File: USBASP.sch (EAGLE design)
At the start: 25 parts, among them IC1 ATMEGA8, IC2 LD111733, J1 Program, J2 Slow clock, J3 USB, J4 ISP Target, J5 VDD Select, Q1 12 MHz

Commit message: Updates for v1.0 release
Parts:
- removed J5: VDD Select, freetronics-luke:JUMPER_SPDT
- added S1: USB, freetronics-jon:USB-6PSMT
- C3: value 22p 0604 -> 22p 0603
- F1: value 500mA PTC -> 500mA PTC 1812
- J1: value Program -> Slow clock
- J2: value Slow clock -> Program
- J3: value USB -> VDD Select; device freetronics-jon:USB-6PSMT -> freetronics-luke:JUMPER_SPDT
- R1: value 10k 0604 -> 10k 0603
- renumbered J4 to S2, Q1 to XTL1
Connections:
- removed net SLOW_SCK: IC1.PC2(ADC2), J2.2
- new net SLOW_CLK: IC1.PC2(ADC2), J1.2
- net !RESET: now also J2.1; no longer J1.1
- net !RESET_OUT: now also J2.2; no longer J1.2
- net +3V3: now also J3.1; no longer J5.1
- net +5V: now also J3.3; no longer J5.3
- net GND: now also J1.1, S1.FIX1, S1.FIX2, S1.GND, S1.PIN1, S1.PIN2, S1.TAB1, S1.TAB2; no longer J2.1, J3.FIX1, J3.FIX2, J3.GND, J3.PIN1, J3.PIN2, J3.TAB1, J3.TAB2
- net N$141: now also S1.VBUS; no longer J3.VBUS
- net N$143: now also S1.D+; no longer J3.D+
- net N$144: now also S1.D-; no longer J3.D-
- net VDD: now also J3.2; no longer J5.2
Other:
- note added: "Freetronics USBASP AVR Programmer"
- note added: "SKU: USBASP"
- note added: "www.freetronics.com/usbasp"
- note removed: "1812"
- note removed: "Freetronics AVR Programmer"
- note removed: "SKU: AVRPROG"
- note removed: "USB Asp Compatible"
- note removed: "www.freetronics.com"
- moved on the sheet: J1, J2, R3

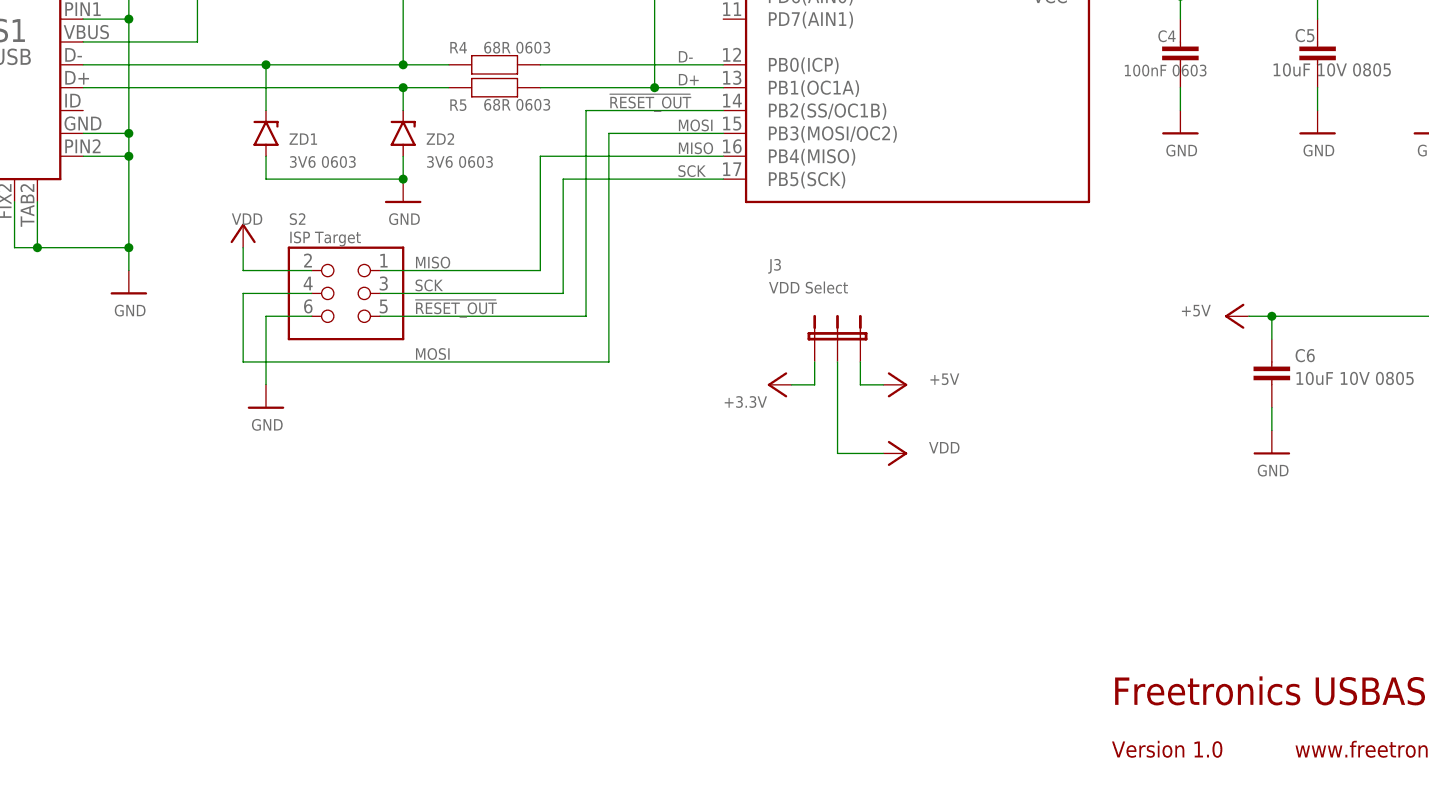
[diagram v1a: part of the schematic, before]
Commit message: Added jumper to enable / disable target power; improved labels
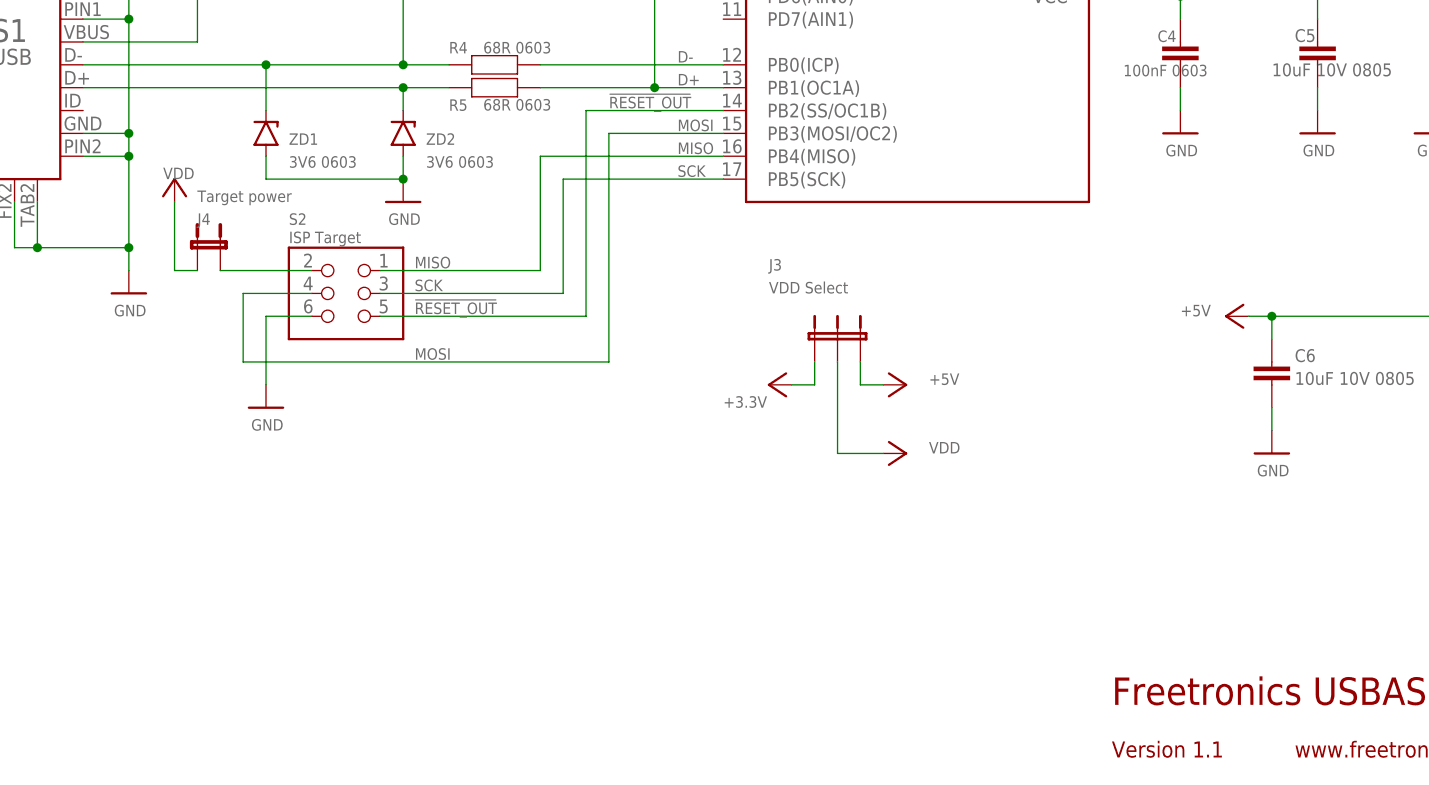
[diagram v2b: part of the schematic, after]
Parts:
- added J4: Target power, freetronics-luke:JUMPER_PTH
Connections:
- new net N$4: J4.2, S2.2
- net VDD: now also J4.1; no longer S2.2
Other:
- note added: "Version 1.1"
- note removed: "Version 1.0"
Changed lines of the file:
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@@
 <part name="J3" library="freetronics-luke" deviceset="JUMPER_SPDT" device="" value="VDD Select"/>
 <part name="U$20" library="freetronics-luke" deviceset="GND" device=""/>
+<part name="J4" library="freetronics-luke" deviceset="JUMPER_PTH" device="" value="Target power"/>
 </parts>
 <sheets>
@@
 <wire x1="119.38" y1="175.26" x2="124.46" y2="175.26" width="0.1524" layer="93"/>
 <text x="147.32" y="12.7" size="3.048" layer="94">Freetronics USBASP AVR Programmer</text>
-<text x="147.32" y="6.858" size="1.778" layer="94">Version 1.0</text>
+<text x="147.32" y="6.858" size="1.778" layer="94">Version 1.1</text>
 <text x="167.64" y="6.858" size="1.778" layer="94">www.freetronics.com/usbasp</text>
 <text x="215.9" y="6.858" size="1.778" layer="94">SKU: USBASP</text>
@@
 <attribute name="VALUE" x="67.31" y="106.68" size="1.27" layer="96"/>
 </instance>
-<instance part="U$15" gate="G$1" x="50.8" y="66.04" smashed="yes">
-<attribute name="VALUE" x="49.53" y="66.04" size="1.27" layer="96"/>
+<instance part="U$15" gate="G$1" x="43.18" y="71.12" smashed="yes">
+<attribute name="VALUE" x="41.91" y="71.12" size="1.27" layer="96"/>
 </instance>
 <instance part="U$2" gate="G$1" x="124.46" y="48.26" smashed="yes" rot="R270">
@@
 <instance part="U$20" gate="G$1" x="38.1" y="58.42" smashed="yes">
 <attribute name="VALUE" x="36.449" y="55.88" size="1.27" layer="96"/>
+</instance>
+<instance part="J4" gate="G$1" x="48.26" y="63.5" smashed="yes">
+<attribute name="NAME" x="45.72" y="66.04" size="1.27" layer="95"/>
+<attribute name="VALUE" x="45.72" y="68.58" size="1.27" layer="96"/>
 </instance>
 </instances>
@@
 </segment>
 <segment>
-<pinref part="S2" gate="G$1" pin="2"/>
-<wire x1="50.8" y1="63.5" x2="50.8" y2="60.96" width="0.1524" layer="91"/>
-<wire x1="50.8" y1="60.96" x2="58.42" y2="60.96" width="0.1524" layer="91"/>
+<wire x1="43.18" y1="68.58" x2="43.18" y2="60.96" width="0.1524" layer="91"/>
 <pinref part="U$15" gate="G$1" pin="VDD"/>
+<pinref part="J4" gate="G$1" pin="1"/>
+<wire x1="45.72" y1="60.96" x2="43.18" y2="60.96" width="0.1524" layer="91"/>
 </segment>
 <segment>
@@
 </segment>
 </net>
+<net name="N$4" class="0">
+<segment>
+<pinref part="S2" gate="G$1" pin="2"/>
+<pinref part="J4" gate="G$1" pin="2"/>
+<wire x1="58.42" y1="60.96" x2="48.26" y2="60.96" width="0.1524" layer="91"/>
+</segment>
+</net>
